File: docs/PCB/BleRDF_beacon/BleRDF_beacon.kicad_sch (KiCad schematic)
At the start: 11 parts, among them J1 Conn_01x02, J2 Conn_01x02, J3 Conn_01x02, J4 Conn_01x02, U1 XIAO-ESP32-C6

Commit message: Update PCB wiring and add 3D case models
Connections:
- net at R3.1: now also U1.8 (GPIO17/D7/RX); no longer U1.10 (GPIO20/D9/MISO)
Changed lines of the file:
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@@
-	)
-	(no_connect
-		(at 149.86 107.95)
 	)
 	(no_connect
@@
 	)
 	(no_connect
+		(at 149.86 100.33)
+	)
+	(no_connect
 		(at 149.86 104.14)
 	)
@@
 	(wire
 		(pts
-			(xy 152.4 100.33) (xy 152.4 107.95)
-		)
-		(stroke
-			(width 0)
-			(type default)
-		)
-	)
-	(wire
-		(pts
 			(xy 170.18 102.87) (xy 182.88 102.87)
 		)
@@
 	(wire
 		(pts
+			(xy 149.86 107.95) (xy 152.4 107.95)
+		)
+		(stroke
+			(width 0)
+			(type default)
+		)
+	)
+	(wire
+		(pts
 			(xy 162.56 88.9) (xy 160.02 88.9)
 		)
@@
 		)
 		(stroke
-			(width 0)
-			(type default)
-		)
-	)
-	(wire
-		(pts
-			(xy 149.86 100.33) (xy 152.4 100.33)
-		)
-		(stroke

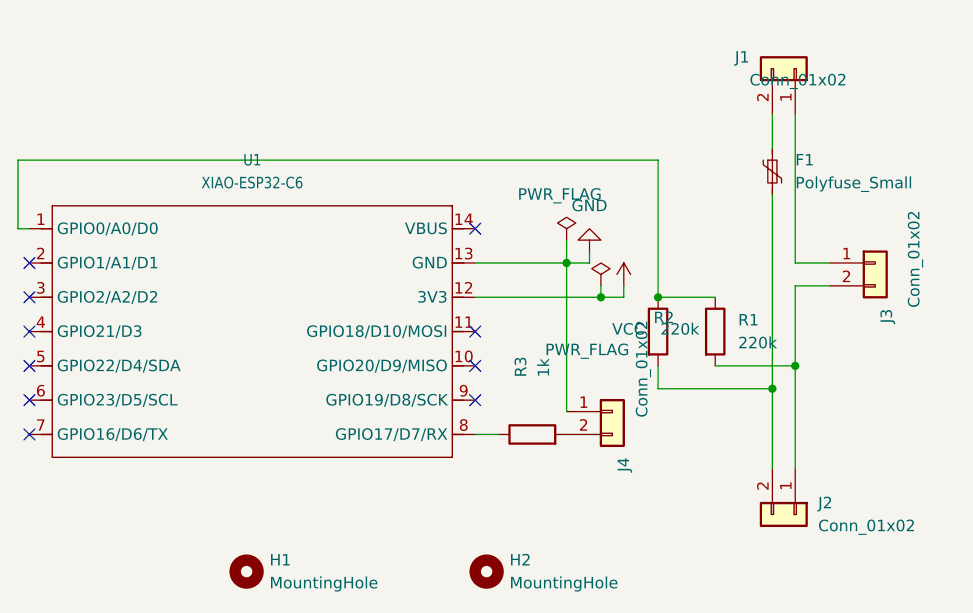
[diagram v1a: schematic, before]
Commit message: Update 3D cases and pcb,hardware documentation
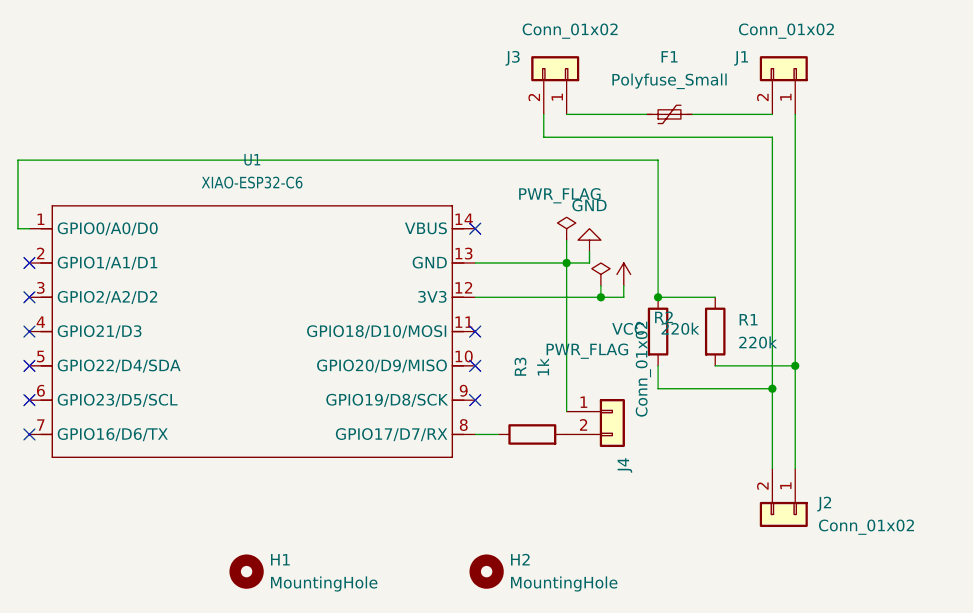
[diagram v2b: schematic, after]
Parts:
- F1: footprint TestPoint:TestPoint_2Pads_Pitch2.54mm_Drill0.8mm -> Capacitor_THT:C_Disc_D4.3mm_W1.9mm_P5.00mm
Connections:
- net at J1.1 (Pin_1): now also J2.1 (Pin_1), R1.2; no longer J3.1 (Pin_1)
- net at J1.2 (Pin_2): now also F1.2; no longer F1.1
- net at J2.2 (Pin_2), R2.2: now also J3.2 (Pin_2); no longer F1.2
- new net: F1.1, J3.1 (Pin_1)
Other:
- moved on the sheet: F1, J3
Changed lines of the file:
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@@
+	)
+	(junction
+		(at 182.88 102.87)
+		(diameter 0)
+		(color 0 0 0 0)
 	)
 	(junction
@@
 	)
 	(junction
-		(at 182.88 102.87)
-		(diameter 0)
-		(color 0 0 0 0)
-	)
-	(junction
 		(at 163.83 92.71)
 		(diameter 0)
@@
 	(wire
 		(pts
-			(xy 182.88 81.28) (xy 182.88 102.87)
-		)
-		(stroke
-			(width 0)
-			(type default)
-		)
-	)
-	(wire
-		(pts
-			(xy 182.88 72.39) (xy 182.88 76.2)
+			(xy 160.02 72.39) (xy 168.91 72.39)
 		)
 		(stroke
@@
 	(wire
 		(pts
-			(xy 185.42 72.39) (xy 185.42 88.9)
+			(xy 185.42 72.39) (xy 185.42 100.33)
 		)
 		(stroke
@@
 	(wire
 		(pts
-			(xy 185.42 91.44) (xy 185.42 100.33)
-		)
-		(stroke
-			(width 0)
-			(type default)
-		)
-	)
-	(wire
-		(pts
 			(xy 99.06 85.09) (xy 100.33 85.09)
 		)
@@
 	(wire
 		(pts
+			(xy 157.48 72.39) (xy 157.48 74.93)
+		)
+		(stroke
+			(width 0)
+			(type default)
+		)
+	)
+	(wire
+		(pts
+			(xy 173.99 72.39) (xy 182.88 72.39)
+		)
+		(stroke
+			(width 0)
+			(type default)
+		)
+	)
+	(wire
+		(pts
 			(xy 163.83 92.71) (xy 166.37 92.71)
 		)
@@
 	(wire
 		(pts
-			(xy 189.23 91.44) (xy 185.42 91.44)
+			(xy 157.48 74.93) (xy 182.88 74.93)
+		)
+		(stroke
+			(width 0)
+			(type default)
+		)
+	)
+	(wire
+		(pts
+			(xy 182.88 74.93) (xy 182.88 102.87)
 		)
 		(stroke
@@
 		(pts
 			(xy 176.53 100.33) (xy 185.42 100.33)
-		)
-		(stroke
-			(width 0)
-			(type default)
-		)
-	)
-	(wire
-		(pts
-			(xy 185.42 88.9) (xy 189.23 88.9)
 		)
 		(stroke
@@
 		)
 		(property "Value" "Conn_01x02"
-			(at 180.34 68.5799 90)
+			(at 179.07 62.992 90)
 			(effects
 				(font
@@
 	(symbol
 		(lib_id "Connector_Generic:Conn_01x02")
-		(at 194.31 88.9 0)
+		(at 160.02 67.31 270)
+		(mirror x)
 		(unit 1)
 		(exclude_from_sim no)
@@
 		(dnp no)
 		(property "Reference" "J3"
-			(at 195.5801 93.98 90)
+			(at 154.94 66.0399 90)
 			(effects
 				(font
@@
 		)
 		(property "Value" "Conn_01x02"
-			(at 198.628 83.058 90)
+			(at 165.862 62.992 90)
 			(effects
 				(font
@@
 		)
 		(property "Footprint" "Connector_JST:JST_XH_B2B-XH-A_1x02_P2.50mm_Vertical"
-			(at 194.31 88.9 0)
+			(at 160.02 67.31 0)
 			(effects
 				(font
@@
 		)
 		(property "Datasheet" "~"
-			(at 194.31 88.9 0)
+			(at 160.02 67.31 0)
 			(effects
 				(font
@@
 		)
 		(property "Description" "Generic connector, single row, 01x02, script generated (kicad-library-utils/schlib/autogen/connector/)"
-			(at 194.31 88.9 0)
+			(at 160.02 67.31 0)
 			(effects
 				(font
@@
 	(symbol
 		(lib_id "Device:Polyfuse_Small")
-		(at 182.88 78.74 0)
+		(at 171.45 72.39 90)
 		(unit 1)
 		(exclude_from_sim no)
@@
 		(fields_autoplaced yes)
 		(property "Reference" "F1"
-			(at 185.42 77.4699 0)
-			(effects
-				(font
-					(size 1.27 1.27)
-				)
-				(justify left)
+			(at 171.45 66.04 90)
+			(effects
+				(font
+					(size 1.27 1.27)
+				)
 			)
 		)
 		(property "Value" "Polyfuse_Small"
-			(at 185.42 80.0099 0)
-			(effects
-				(font
-					(size 1.27 1.27)
-				)
-				(justify left)
-			)
-		)
-		(property "Footprint" "TestPoint:TestPoint_2Pads_Pitch2.54mm_Drill0.8mm"
-			(at 184.15 83.82 0)
+			(at 171.45 68.58 90)
+			(effects
+				(font
+					(size 1.27 1.27)
+				)
+			)
+		)
+		(property "Footprint" "Capacitor_THT:C_Disc_D4.3mm_W1.9mm_P5.00mm"
+			(at 176.53 71.12 0)
 			(effects
 				(font
@@
 		)
 		(property "Datasheet" "~"
-			(at 182.88 78.74 0)
+			(at 171.45 72.39 0)
 			(effects
 				(font
@@
 		)
 		(property "Description" "Resettable fuse, polymeric positive temperature coefficient, small symbol"
-			(at 182.88 78.74 0)
-			(effects
-				(font
+			(at 171.45 72.39 0)
+			(effects
+				(font

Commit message: Fix LED Connector Directon BleRDF_Beacon PCB
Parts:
- R3: footprint Resistor_THT:R_Axial_DIN0204_L3.6mm_D1.6mm_P7.62mm_Horizontal -> Resistor_THT:R_Axial_DIN0207_L6.3mm_D2.5mm_P7.62mm_Horizontal
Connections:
- net GND: now also J4.2 (Pin_2); no longer J4.1 (Pin_1)
- net at R3.2: now also J4.1 (Pin_1); no longer J4.2 (Pin_2)
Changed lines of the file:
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@@
+	(wire
+		(pts
+			(xy 160.02 88.9) (xy 160.02 105.41)
+		)
+		(stroke
+			(width 0)
+			(type default)
+		)
+	)
 	(wire
 		(pts
@@
 		(pts
 			(xy 149.86 88.9) (xy 160.02 88.9)
-		)
-		(stroke
-			(width 0)
-			(type default)
-		)
-	)
-	(wire
-		(pts
-			(xy 160.02 88.9) (xy 160.02 105.41)
 		)
 		(stroke
@@
 	(symbol
 		(lib_id "Connector_Generic:Conn_01x02")
-		(at 165.1 105.41 0)
+		(at 165.1 107.95 0)
+		(mirror x)
 		(unit 1)
 		(exclude_from_sim no)
@@
 		(dnp no)
 		(property "Reference" "J4"
-			(at 166.3701 110.49 90)
+			(at 166.3701 102.87 90)
 			(effects
 				(font
@@
 		)
 		(property "Value" "Conn_01x02"
-			(at 168.402 95.25 90)
+			(at 168.402 118.11 90)
 			(effects
 				(font
@@
 		)
 		(property "Footprint" "Connector_JST:JST_XH_B2B-XH-A_1x02_P2.50mm_Vertical"
-			(at 165.1 105.41 0)
+			(at 165.1 107.95 0)
 			(effects
 				(font
@@
 		)
 		(property "Datasheet" "~"
-			(at 165.1 105.41 0)
+			(at 165.1 107.95 0)
 			(effects
 				(font
@@
 		)
 		(property "Description" "Generic connector, single row, 01x02, script generated (kicad-library-utils/schlib/autogen/connector/)"
-			(at 165.1 105.41 0)
+			(at 165.1 107.95 0)
 			(effects
 				(font
@@
 			)
 		)
-		(property "Footprint" "Resistor_THT:R_Axial_DIN0204_L3.6mm_D1.6mm_P7.62mm_Horizontal"
+		(property "Footprint" "Resistor_THT:R_Axial_DIN0207_L6.3mm_D2.5mm_P7.62mm_Horizontal"
 			(at 156.21 109.728 90)
 			(effects
